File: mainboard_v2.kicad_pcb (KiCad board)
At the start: 4 copper layers, 156.9 x 46 mm, 38 parts, among them J1 PWR_IN, J2 CLK_IN, J3 Conn_01x50, SW1 RESET, U1 DS1813, U2 W65C02SxP, U3 74HC21, U4 CY62256-70PC, U5 28C256, U6 74HC133, U7 74HC04, U8 74HC00, U9 74HC138, X1 ACO-xxxMHz

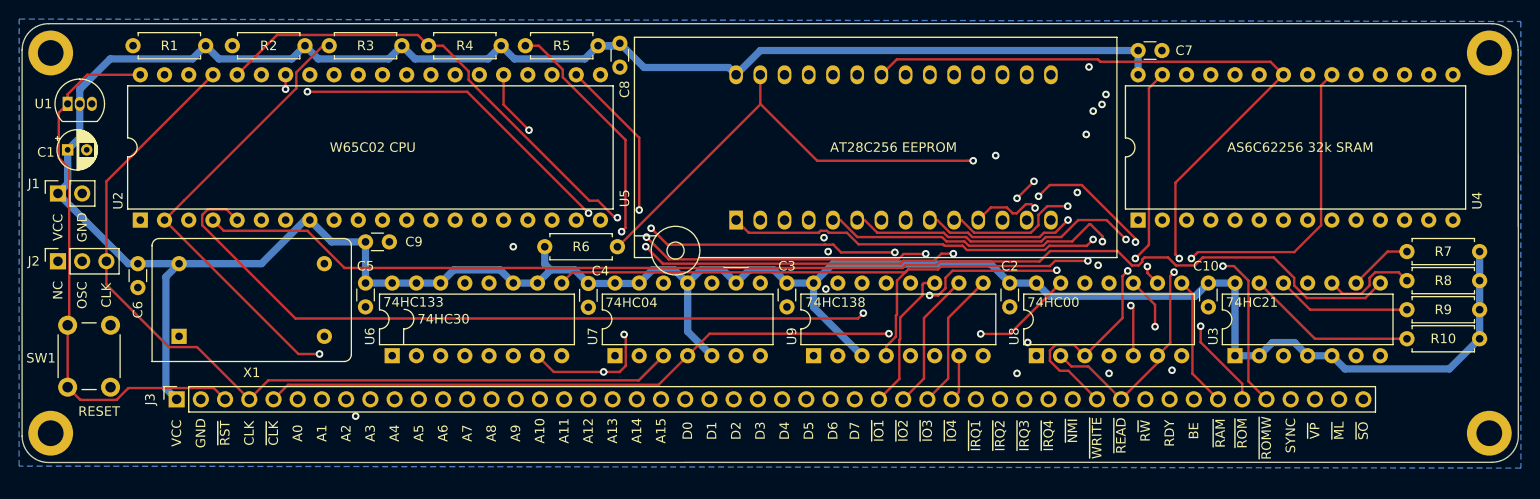
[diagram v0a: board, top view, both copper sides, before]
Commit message: Update for KiCad 6
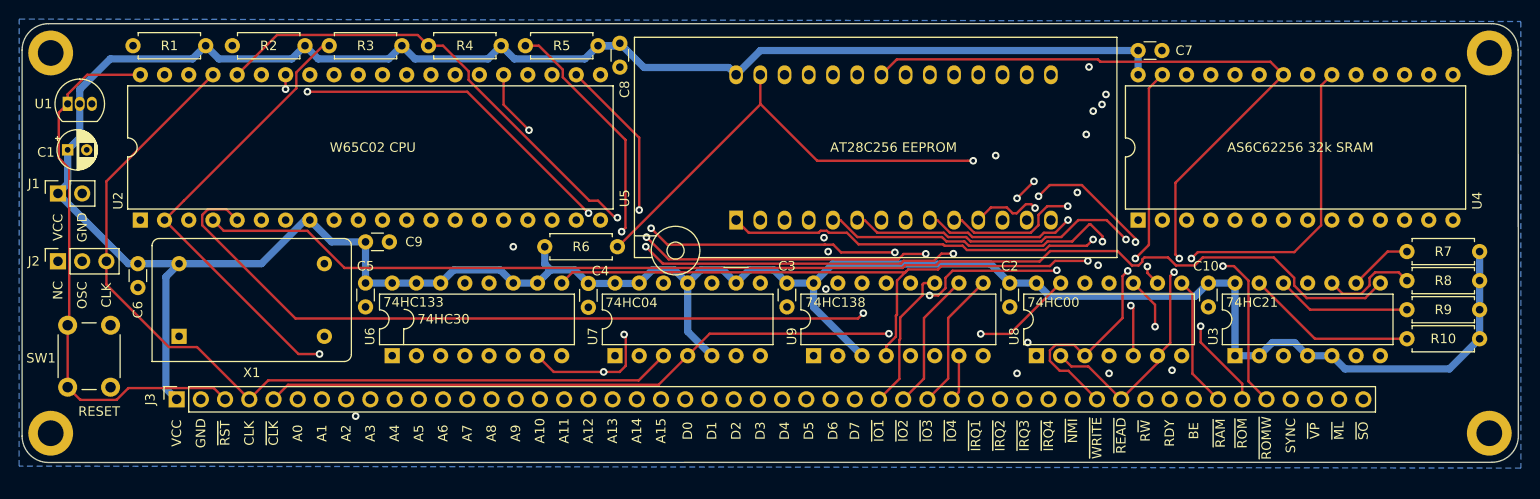
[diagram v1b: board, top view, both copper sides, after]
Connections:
- net BE renamed /BE
- net CLK renamed /CLK
- net IO1 renamed /IO1
- net IO2 renamed /IO2
- net IO3 renamed /IO3
- net IO4 renamed /IO4
- net IRQ renamed /IRQ
- net IRQ1 renamed /IRQ1
- net IRQ2 renamed /IRQ2
- net IRQ3 renamed /IRQ3
- net IRQ4 renamed /IRQ4
- net ML renamed /ML
- net NMI renamed /NMI
- net RAM_~CS renamed /RAM_~{CS}
- net RDY renamed /RDY
- net ROM_~CS renamed /ROM_~{CS}
- net ROM_~WE renamed /ROM_~{WE}
- net RST renamed /RST
- net RW renamed /RW
- net SO renamed /SO
- net SYNC renamed /SYNC
- net VP renamed /VP
- net ~CLK renamed /~{CLK}
- net ~READ renamed /~{READ}
- net ~WRITE renamed /~{WRITE}
- J2 pad 1: (no net) -> unconnected-(J2-Pad1)
- U2 pad 3: (no net) -> unconnected-(U2-Pad3)
- U2 pad 35: (no net) -> unconnected-(U2-Pad35)
- U2 pad 39: (no net) -> unconnected-(U2-Pad39)
- U3 pad 6: (no net) -> unconnected-(U3-Pad6)
- U7 pad 10: (no net) -> unconnected-(U7-Pad10)
- U7 pad 12: (no net) -> unconnected-(U7-Pad12)
- U7 pad 6: (no net) -> unconnected-(U7-Pad6)
- U7 pad 8: (no net) -> unconnected-(U7-Pad8)
- U9 pad 12: (no net) -> unconnected-(U9-Pad12)
- U9 pad 13: (no net) -> unconnected-(U9-Pad13)
- U9 pad 14: (no net) -> unconnected-(U9-Pad14)
- U9 pad 15: (no net) -> unconnected-(U9-Pad15)
- X1 pad 1: (no net) -> unconnected-(X1-Pad1)
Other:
- net class Default removed
- board text added: "R~{W}"
- board text added: "~{CLK}"
- board text added: "~{IO1}"
- board text added: "~{IO2}"
- board text added: "~{IO3}"
- board text added: "~{IO4}"
- board text added: "~{IRQ1}"
- board text added: "~{IRQ2}"
- board text added: "~{IRQ3}"
- board text added: "~{IRQ4}"
- board text added: "~{ML}"
- board text added: "~{NMI}"
- board text added: "~{RAM}"
- board text added: "~{READ}"
- board text added: "~{ROMW}"
- board text added: "~{ROM}"
- board text added: "~{RST}"
- board text added: "~{SO}"
- board text added: "~{VP}"
- board text added: "~{WRITE}"
- board text removed: "R~W"
- board text removed: "~CLK"
- board text removed: "~IO1"
- board text removed: "~IO2"
- board text removed: "~IO3"
- board text removed: "~IO4"
- board text removed: "~IRQ1"
- board text removed: "~IRQ2"
- board text removed: "~IRQ3"
- board text removed: "~IRQ4"
- board text removed: "~ML"
- board text removed: "~NMI"
- board text removed: "~RAM"
- board text removed: "~READ"
- board text removed: "~ROM"
- board text removed: "~ROMW"
- board text removed: "~RST"
- board text removed: "~SO"
- board text removed: "~VP"
- board text removed: "~WRITE"
